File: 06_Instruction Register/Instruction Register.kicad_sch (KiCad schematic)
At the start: 5 parts, among them J1 Data bus, J2 Instruction Bus, J3 Step-Flag Bus, J4 Input 1, J5 Input 2

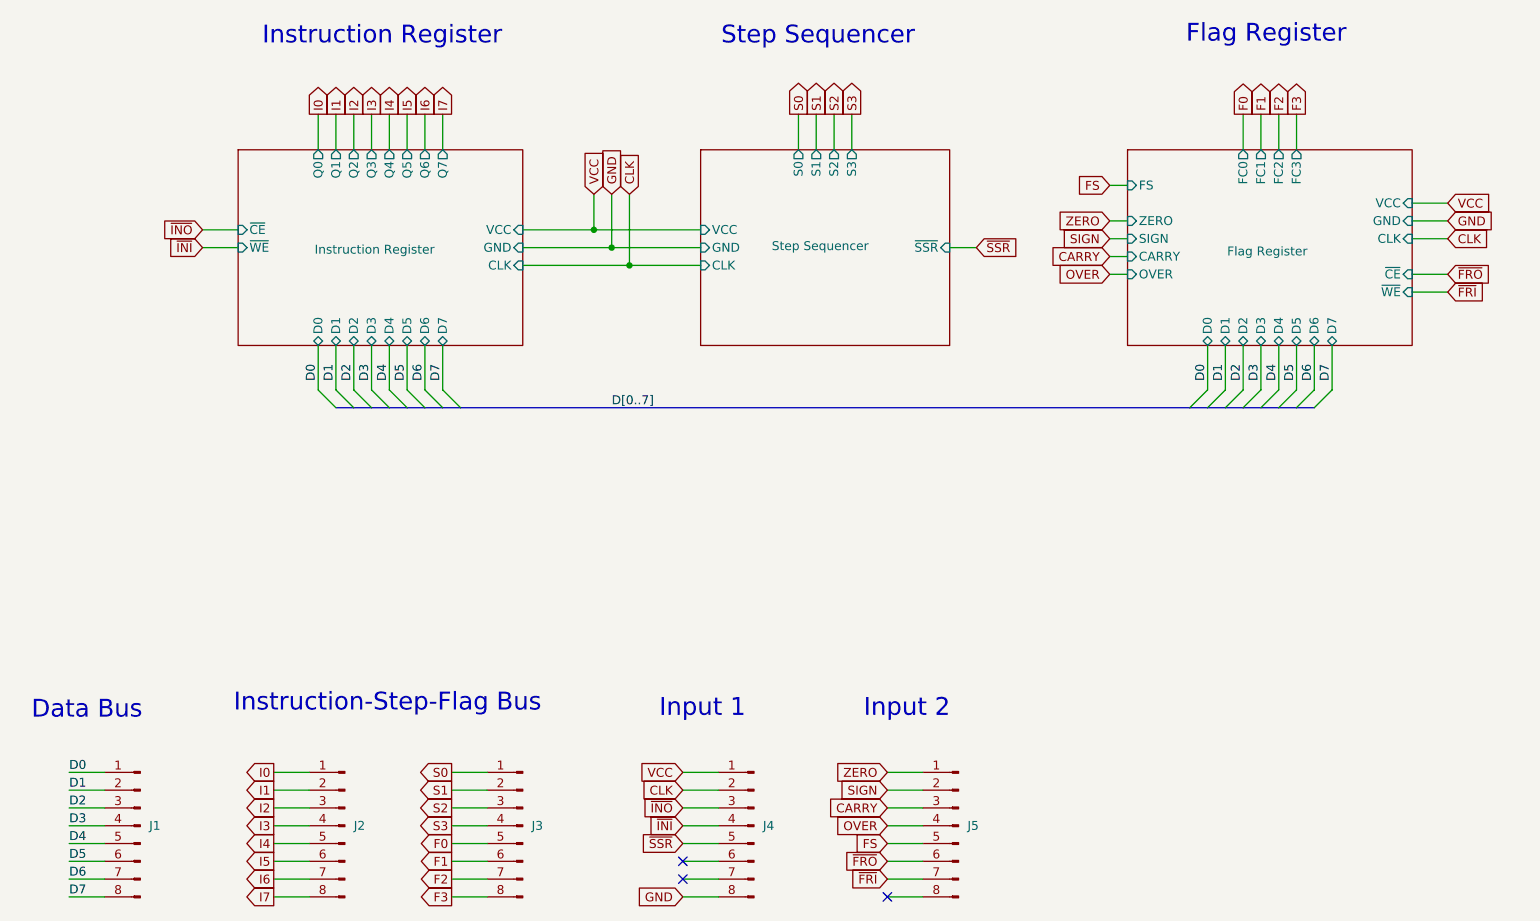
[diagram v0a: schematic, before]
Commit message: Last revision of the cpu, all boards have been ordered. Implementation to be tested and documented in following commits.
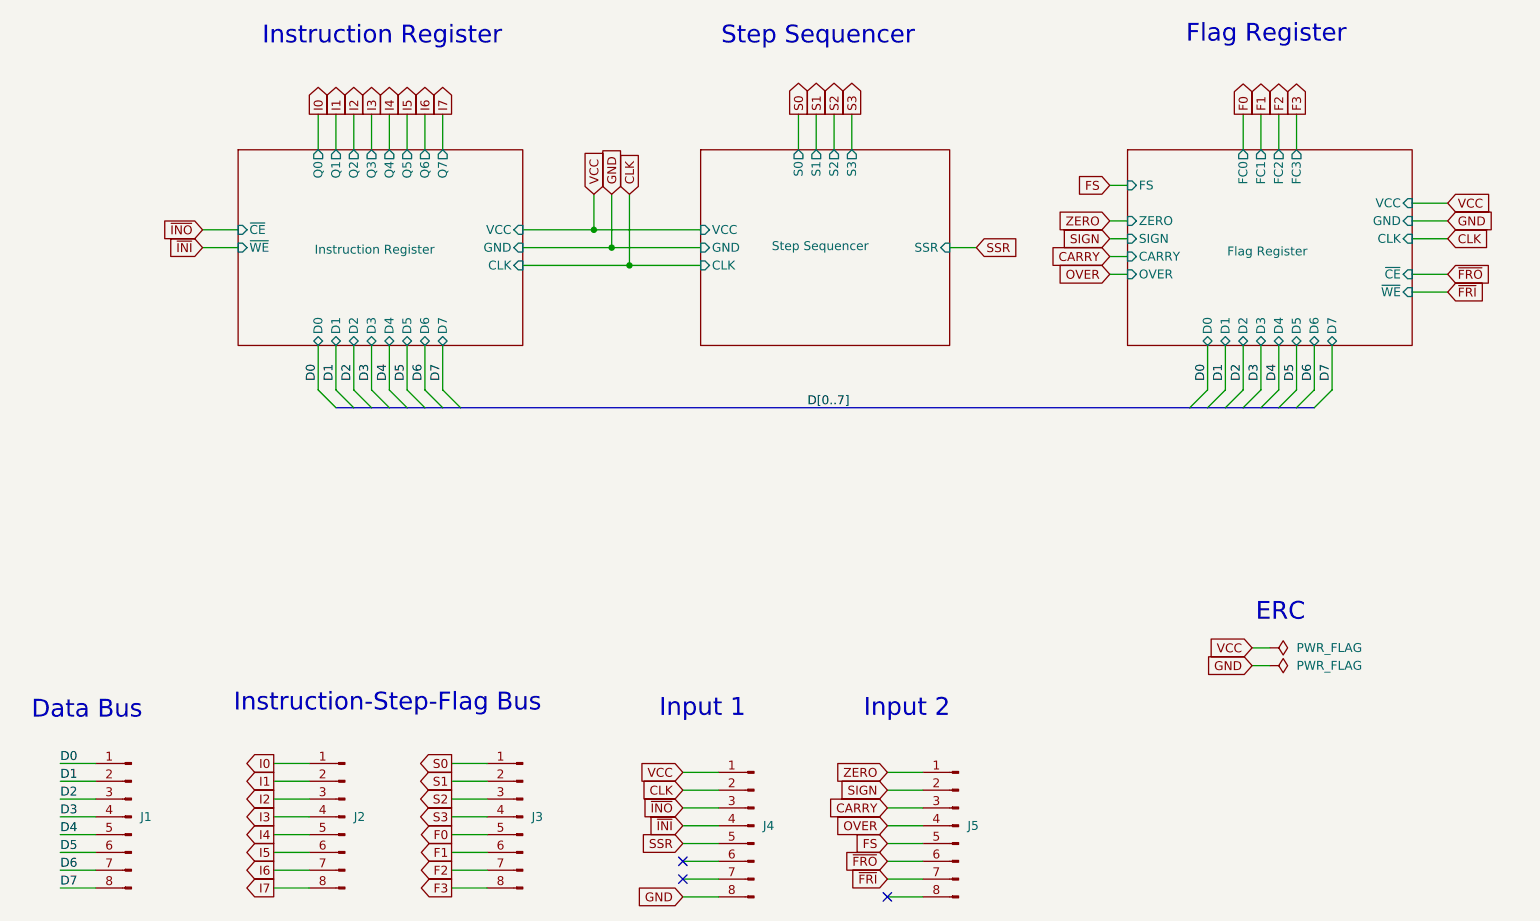
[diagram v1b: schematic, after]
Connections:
- net ~{SSR} renamed SSR
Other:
- sheet Step Sequencer ports: added SSR; removed ~{SSR}
- note added: "ERC"
- moved on the sheet: J1, J2, J3

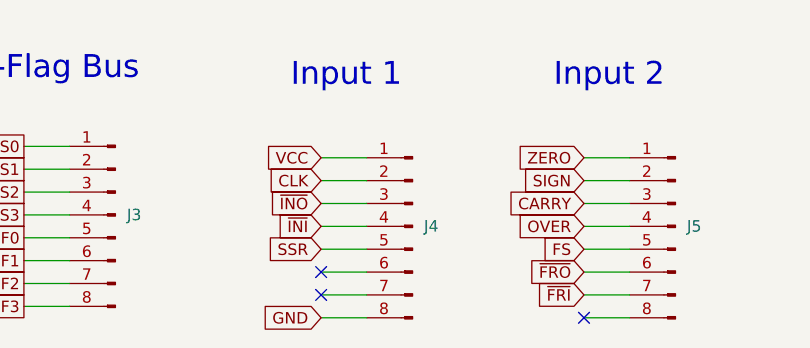
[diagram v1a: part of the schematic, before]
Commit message: Instruction register v1.11 Corrected label ~{SSR} to SSR, no modification to the circuit itself. Active low and high inputs swapped from Input2 to Input1.
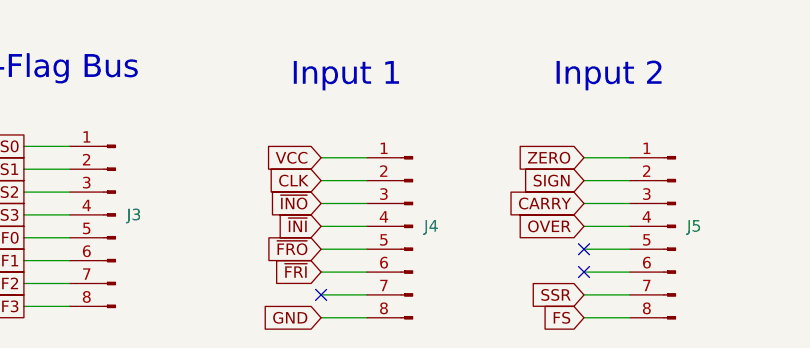
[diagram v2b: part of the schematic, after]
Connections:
- net FS: now also J5.8 (Pin_8); no longer J5.5 (Pin_5)
- net SSR: now also J5.7 (Pin_7); no longer J4.5 (Pin_5)
- net ~{FRI}: now also J4.6 (Pin_6); no longer J5.7 (Pin_7)
- net ~{FRO}: now also J4.5 (Pin_5); no longer J5.6 (Pin_6)
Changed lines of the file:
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@@
 	(title_block
 		(title "Instruction Register")
-		(date "2025-11-14")
-		(rev "1.0")
+		(date "2026-01-04")
+		(rev "1.11")
 		(company "Marco Vettigli")
 	)
@@
 	)
 	(no_connect
-		(at 123.19 187.96)
+		(at 123.19 190.5)
 	)
 	(no_connect
-		(at 123.19 190.5)
+		(at 152.4 185.42)
 	)
 	(no_connect
-		(at 152.4 193.04)
+		(at 152.4 187.96)
 	)
 	(bus_entry
@@
 	(global_label "FS"
 		(shape input)
-		(at 152.4 185.42 180)
+		(at 152.4 193.04 180)
 		(fields_autoplaced yes)
 		(effects
@@
 		)
 		(property "Intersheetrefs" "${INTERSHEET_REFS}"
-			(at 147.1167 185.42 0)
+			(at 147.1167 193.04 0)
 			(effects
 				(font
@@
 	(global_label "SSR"
 		(shape input)
-		(at 123.19 185.42 180)
+		(at 152.4 190.5 180)
 		(fields_autoplaced yes)
 		(effects
@@
 		)
 		(property "Intersheetrefs" "${INTERSHEET_REFS}"
-			(at 116.5158 185.42 0)
+			(at 145.7258 190.5 0)
 			(effects
 				(font
@@
 	(global_label "~{FRO}"
 		(shape input)
-		(at 152.4 187.96 180)
+		(at 123.19 185.42 180)
 		(fields_autoplaced yes)
 		(effects
@@
 		)
 		(property "Intersheetrefs" "${INTERSHEET_REFS}"
-			(at 145.7257 187.96 0)
+			(at 116.5157 185.42 0)
 			(effects
 				(font
@@
 	(global_label "~{FRI}"
 		(shape input)
-		(at 152.4 190.5 180)
+		(at 123.19 187.96 180)
 		(fields_autoplaced yes)
 		(effects
@@
 		)
 		(property "Intersheetrefs" "${INTERSHEET_REFS}"
-			(at 146.4514 190.5 0)
+			(at 117.2414 187.96 0)
 			(effects
 				(font
